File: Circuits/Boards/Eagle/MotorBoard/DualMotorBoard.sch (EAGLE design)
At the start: 94 parts, among them M1 IRFS7537PBF, M2 IRFS7537PBF, M3 IRFS7537PBF, M4 IRFS7537PBF, M5 IRFS7537PBF, M6 IRFS7537PBF, M7 IRFS7537PBF, M8 IRFS7537PBF, Q1 2N3904, Q10 2N3904, Q11 2N3904, Q12 2N3904, Q13 2N3904, Q14 2N3904, Q15 2N3904, Q16 2N3904, Q2 2N3904, Q3 2N3904, Q4 2N3904, Q5 2N3904, Q6 2N3904, Q7 2N3904, Q8 2N3904, Q9 2N3904

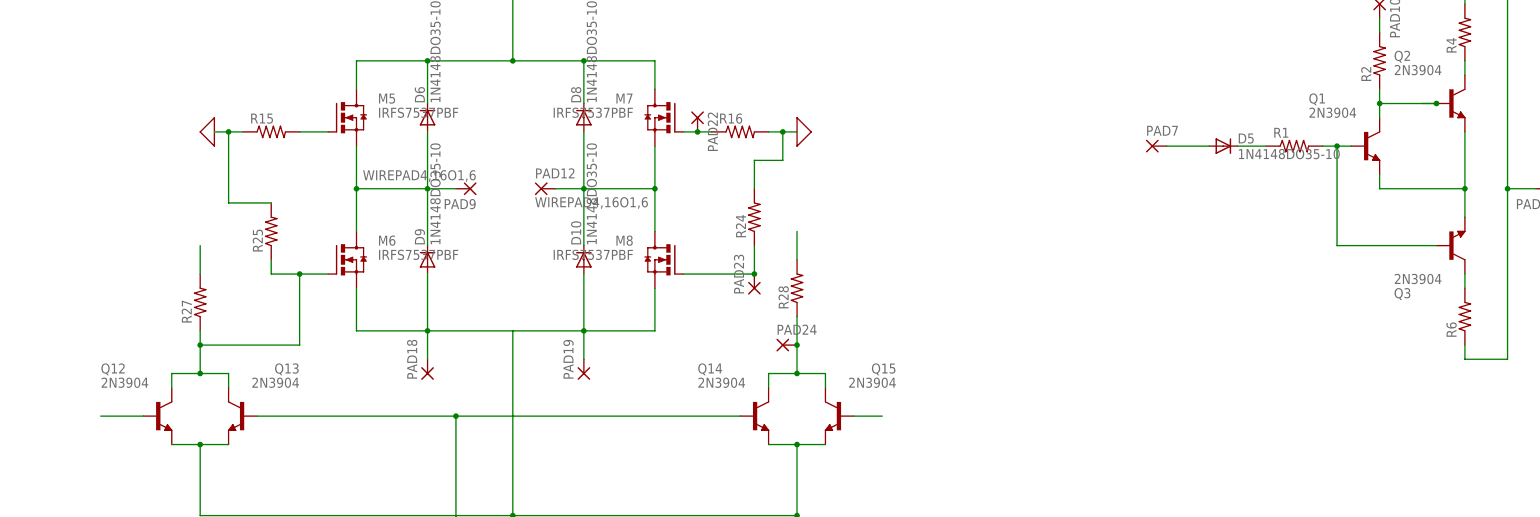
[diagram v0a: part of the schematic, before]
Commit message: Update KiCAD motor controller and Version 2 simulation
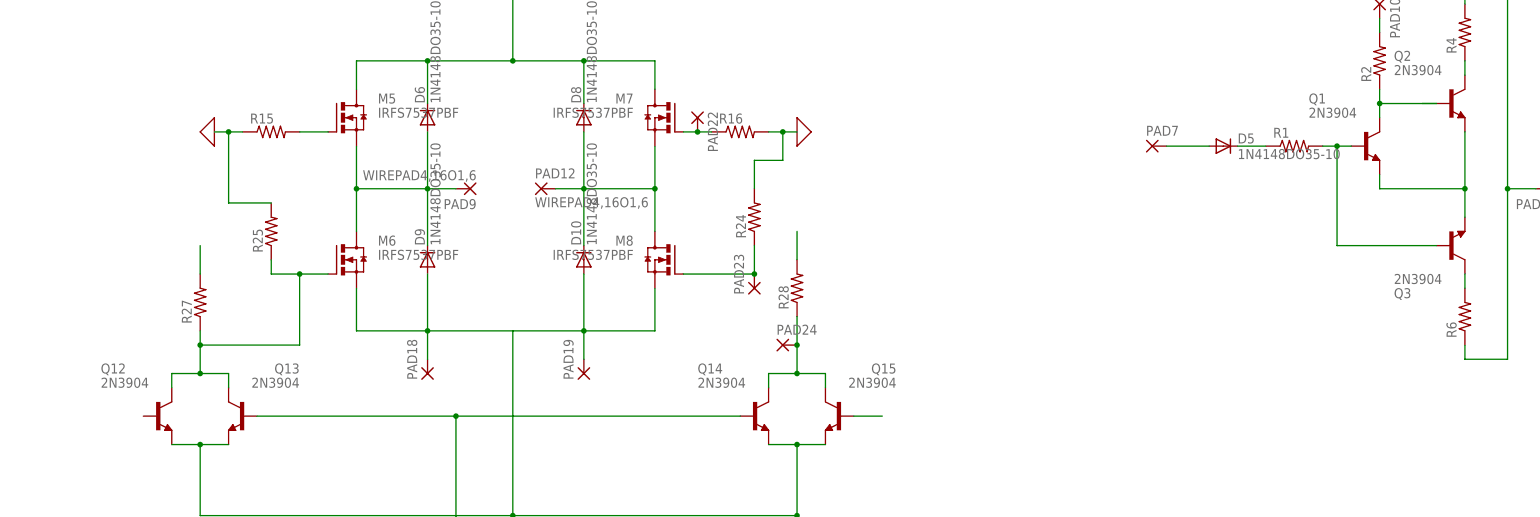
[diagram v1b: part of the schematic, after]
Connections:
- net BB1: no longer Q12.B
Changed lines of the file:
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@@
 <wire x1="-7.62" y1="129.54" x2="-5.08" y2="129.54" width="0.1524" layer="91"/>
 <wire x1="-15.24" y1="129.54" x2="-5.08" y2="129.54" width="0.1524" layer="91"/>
-<junction x="-5.08" y="129.54"/>
 </segment>
 <segment>
@@
 <pinref part="Q11" gate="G1" pin="B"/>
 </segment>
-<segment>
-<pinref part="Q12" gate="G1" pin="B"/>
-<wire x1="-236.22" y1="73.66" x2="-243.84" y2="73.66" width="0.1524" layer="91"/>
-</segment>
-</net>
+</net>
